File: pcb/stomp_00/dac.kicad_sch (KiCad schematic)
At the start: 6 parts, among them J4 Headphones, U9 SGTL5000XNAA3

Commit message: taking shape...
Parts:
- R1, R2, R3: footprint (none) -> Resistor_SMD:R_0603_1608Metric
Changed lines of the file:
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@@
       (effects (font (size 1.27 1.27)))
     )
-    (property "Footprint" "" (at 125.476 94.996 90)
+    (property "Footprint" "Resistor_SMD:R_0603_1608Metric" (at 125.476 94.996 90)
       (effects (font (size 1.27 1.27)) hide)
     )
@@
       (effects (font (size 1.27 1.27)) (justify right))
     )
-    (property "Footprint" "" (at 99.314 106.426 90)
+    (property "Footprint" "Resistor_SMD:R_0603_1608Metric" (at 99.314 106.426 90)
       (effects (font (size 1.27 1.27)) hide)
     )
@@
       (effects (font (size 1.27 1.27)) (justify right))
     )
-    (property "Footprint" "" (at 90.424 106.426 90)
+    (property "Footprint" "Resistor_SMD:R_0603_1608Metric" (at 90.424 106.426 90)
       (effects (font (size 1.27 1.27)) hide)
     )

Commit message: seeing whether everything will fit...
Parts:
- J4: footprint (none) -> Connector_PinHeader_2.54mm:PinHeader_1x03_P2.54mm_Vertical
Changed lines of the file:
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@@
       (effects (font (size 1.27 1.27)) (justify right))
     )
-    (property "Footprint" "" (at 173.99 86.36 0)
+    (property "Footprint" "Connector_PinHeader_2.54mm:PinHeader_1x03_P2.54mm_Vertical" (at 173.99 86.36 0)
       (effects (font (size 1.27 1.27)) hide)
     )

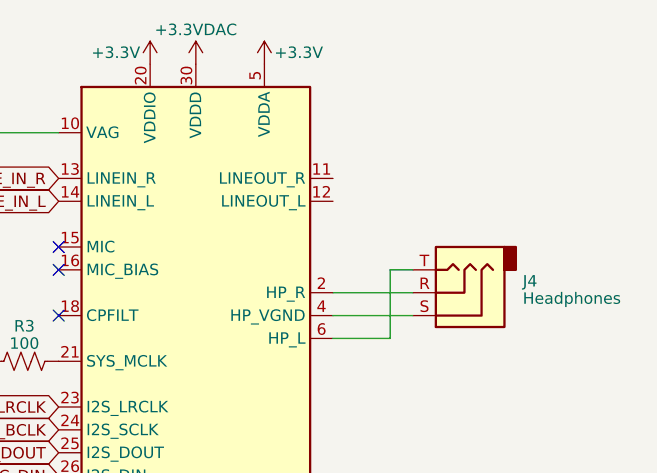
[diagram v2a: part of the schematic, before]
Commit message: input stage schematic
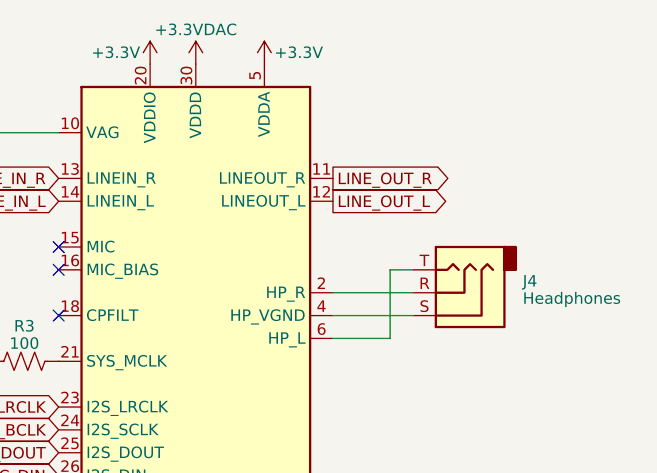
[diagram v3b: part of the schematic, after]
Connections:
- net LINE_OUT_R: now reaches U9.11 (LINEOUT_R)
- net LINE_OUT_L: now reaches U9.12 (LINEOUT_L)
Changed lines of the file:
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@@
     (stroke (width 0) (type default))
+  )
+  (global_label "LINE_OUT_L" (shape output) (at 160.02 76.2 0) (fields_autoplaced)
+    (effects (font (size 1.27 1.27)) (justify left))
+    (property "Intersheetrefs" "${INTERSHEET_REFS}" (at 173.6301 76.2 0)
+      (effects (font (size 1.27 1.27)) (justify left) hide)
+    )
   )
   (global_label "DAC_SCL" (shape input) (at 88.9 114.3 180) (fields_autoplaced)
@@
     )
   )
+  (global_label "LINE_OUT_R" (shape output) (at 160.02 73.66 0) (fields_autoplaced)
+    (effects (font (size 1.27 1.27)) (justify left))
+    (property "Intersheetrefs" "${INTERSHEET_REFS}" (at 173.872 73.66 0)
+      (effects (font (size 1.27 1.27)) (justify left) hide)
+    )
+  )

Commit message: more input stage faffing
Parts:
- added C19, C20, C21, C22: 2.2uF, symbol Device:C_Polarized_US
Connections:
- net LINE_IN_L: now also C20.2; no longer U9.14 (LINEIN_L)
- net LINE_IN_R: now also C19.2; no longer U9.13 (LINEIN_R)
- net LINE_OUT_L: now also C22.2; no longer U9.12 (LINEOUT_L)
- net LINE_OUT_R: now also C21.2; no longer U9.11 (LINEOUT_R)
- new net: C21.1, U9.11 (LINEOUT_R)
- new net: C22.1, U9.12 (LINEOUT_L)
- new net: C19.1, U9.13 (LINEIN_R)
- new net: C20.1, U9.14 (LINEIN_L)
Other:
- moved on the sheet: C6
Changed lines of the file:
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@@
+    (stroke (width 0) (type default))
+  )
+  (wire (pts (xy 160.02 73.66) (xy 198.12 73.66))
     (stroke (width 0) (type default))
   )
@@
     (stroke (width 0) (type default))
   )
+  (wire (pts (xy 110.49 81.915) (xy 115.57 81.915))
+    (stroke (width 0) (type default))
+  )
   (wire (pts (xy 100.33 110.49) (xy 100.33 114.3))
     (stroke (width 0) (type default))
@@
     (stroke (width 0) (type default))
   )
+  (wire (pts (xy 110.49 73.66) (xy 129.54 73.66))
+    (stroke (width 0) (type default))
+  )
   (wire (pts (xy 160.02 91.44) (xy 166.37 91.44))
     (stroke (width 0) (type default))
@@
     (stroke (width 0) (type default))
   )
-  (wire (pts (xy 101.6 68.58) (xy 129.54 68.58))
+  (wire (pts (xy 115.57 76.2) (xy 129.54 76.2))
+    (stroke (width 0) (type default))
+  )
+  (wire (pts (xy 77.47 68.58) (xy 129.54 68.58))
     (stroke (width 0) (type default))
   )
@@
     (stroke (width 0) (type default))
   )
+  (wire (pts (xy 196.215 76.2) (xy 196.215 81.915))
+    (stroke (width 0) (type default))
+  )
+  (wire (pts (xy 160.02 76.2) (xy 196.215 76.2))
+    (stroke (width 0) (type default))
+  )
+  (wire (pts (xy 115.57 76.2) (xy 115.57 81.915))
+    (stroke (width 0) (type default))
+  )
   (wire (pts (xy 166.37 83.82) (xy 168.91 83.82))
     (stroke (width 0) (type default))
@@
     (stroke (width 0) (type default))
   )
+  (wire (pts (xy 196.215 81.915) (xy 198.12 81.915))
+    (stroke (width 0) (type default))
+  )
   (wire (pts (xy 88.9 114.3) (xy 100.33 114.3))
     (stroke (width 0) (type default))
@@
     (stroke (width 0) (type default))
   )
-  (global_label "LINE_OUT_L" (shape output) (at 160.02 76.2 0) (fields_autoplaced)
+  (text_box "Check that this matches the Teensy Audio schematic, doesn't currently!"
+    (at 110.49 35.56 0) (size 37.465 15.24)
+    (stroke (width 0) (type default))
+    (fill (type none))
+    (effects (font (size 1.27 1.27)) (justify left top))
+  )
+  (global_label "LINE_OUT_L" (shape output) (at 205.74 81.915 0) (fields_autoplaced)
     (effects (font (size 1.27 1.27)) (justify left))
-    (property "Intersheetrefs" "${INTERSHEET_REFS}" (at 173.6301 76.2 0)
+    (property "Intersheetrefs" "${INTERSHEET_REFS}" (at 219.3501 81.915 0)
       (effects (font (size 1.27 1.27)) (justify left) hide)
     )
@@
     )
   )
-  (global_label "LINE_OUT_R" (shape output) (at 160.02 73.66 0) (fields_autoplaced)
+  (global_label "LINE_OUT_R" (shape output) (at 205.74 73.66 0) (fields_autoplaced)
     (effects (font (size 1.27 1.27)) (justify left))
-    (property "Intersheetrefs" "${INTERSHEET_REFS}" (at 173.872 73.66 0)
+    (property "Intersheetrefs" "${INTERSHEET_REFS}" (at 219.592 73.66 0)
       (effects (font (size 1.27 1.27)) (justify left) hide)
     )
   )
-  (global_label "LINE_IN_R" (shape input) (at 129.54 73.66 180) (fields_autoplaced)
-    (effects (font (size 1.27 1.27)) (justify right))
-    (property "Intersheetrefs" "${INTERSHEET_REFS}" (at 117.3813 73.66 0)
+  (global_label "LINE_IN_R" (shape input) (at 102.87 73.66 180) (fields_autoplaced)
+    (effects (font (size 1.27 1.27)) (justify right))
+    (property "Intersheetrefs" "${INTERSHEET_REFS}" (at 90.7113 73.66 0)
       (effects (font (size 1.27 1.27)) (justify right) hide)
     )
@@
     )
   )
-  (global_label "LINE_IN_L" (shape input) (at 129.54 76.2 180) (fields_autoplaced)
-    (effects (font (size 1.27 1.27)) (justify right))
-    (property "Intersheetrefs" "${INTERSHEET_REFS}" (at 117.6232 76.2 0)
+  (global_label "LINE_IN_L" (shape input) (at 102.87 81.915 180) (fields_autoplaced)
+    (effects (font (size 1.27 1.27)) (justify right))
+    (property "Intersheetrefs" "${INTERSHEET_REFS}" (at 90.9532 81.915 0)
       (effects (font (size 1.27 1.27)) (justify right) hide)
     )
@@
     )
   )
-  (symbol (lib_id "Device:C_Polarized_US") (at 101.6 72.39 0) (unit 1)
-    (in_bom yes) (on_board yes) (dnp no) (fields_autoplaced)
-    (property "Reference" "C6" (at 104.521 71.1113 0)
+  (symbol (lib_id "Device:C_Polarized_US") (at 77.47 72.39 0) (unit 1)
+    (in_bom yes) (on_board yes) (dnp no) (fields_autoplaced)
+    (property "Reference" "C6" (at 80.391 71.1113 0)
       (effects (font (size 1.27 1.27)) (justify left))
     )
-    (property "Value" "150nF" (at 104.521 73.0323 0)
+    (property "Value" "150nF" (at 80.391 73.0323 0)
       (effects (font (size 1.27 1.27)) (justify left))
     )
-    (property "Footprint" "" (at 101.6 72.39 0)
-      (effects (font (size 1.27 1.27)) hide)
-    )
-    (property "Datasheet" "~" (at 101.6 72.39 0)
+    (property "Footprint" "" (at 77.47 72.39 0)
+      (effects (font (size 1.27 1.27)) hide)
+    )
+    (property "Datasheet" "~" (at 77.47 72.39 0)
       (effects (font (size 1.27 1.27)) hide)
     )
@@
         (path "/8f4a2eb0-078b-46cb-b534-a4acd11d130e/7598c0f0-0137-4b50-80b5-b929d25c284a"
           (reference "C6") (unit 1)
+        )
+      )
+    )
+  )
+  (symbol (lib_id "Device:C_Polarized_US") (at 106.68 81.915 270) (unit 1)
+    (in_bom yes) (on_board yes) (dnp no) (fields_autoplaced)
+    (property "Reference" "C20" (at 107.315 76.7461 90)
+      (effects (font (size 1.27 1.27)))
+    )
+    (property "Value" "2.2uF" (at 107.315 78.6671 90)
+      (effects (font (size 1.27 1.27)))
+    )
+    (property "Footprint" "" (at 106.68 81.915 0)
+      (effects (font (size 1.27 1.27)) hide)
+    )
+    (property "Datasheet" "~" (at 106.68 81.915 0)
+      (effects (font (size 1.27 1.27)) hide)
+    )
+    (pin "1")
+    (pin "2")
+    (instances
+      (project "stomp_00"
+        (path "/8f4a2eb0-078b-46cb-b534-a4acd11d130e/7598c0f0-0137-4b50-80b5-b929d25c284a"
+          (reference "C20") (unit 1)
+        )
+      )
+    )
+  )
+  (symbol (lib_id "Device:C_Polarized_US") (at 201.93 73.66 90) (mirror x) (unit 1)
+    (in_bom yes) (on_board yes) (dnp no) (fields_autoplaced)
+    (property "Reference" "C21" (at 201.295 68.4911 90)
+      (effects (font (size 1.27 1.27)))
+    )
+    (property "Value" "2.2uF" (at 201.295 70.4121 90)
+      (effects (font (size 1.27 1.27)))
+    )
+    (property "Footprint" "" (at 201.93 73.66 0)
+      (effects (font (size 1.27 1.27)) hide)
+    )
+    (property "Datasheet" "~" (at 201.93 73.66 0)
+      (effects (font (size 1.27 1.27)) hide)
+    )
+    (pin "1")
+    (pin "2")
+    (instances
+      (project "stomp_00"
+        (path "/8f4a2eb0-078b-46cb-b534-a4acd11d130e/7598c0f0-0137-4b50-80b5-b929d25c284a"
+          (reference "C21") (unit 1)
         )
       )
@@
     )
   )
-  (symbol (lib_id "power:GND") (at 101.6 76.2 0) (unit 1)
-    (in_bom yes) (on_board yes) (dnp no) (fields_autoplaced)
-    (property "Reference" "#PWR011" (at 101.6 82.55 0)
-      (effects (font (size 1.27 1.27)) hide)
-    )
-    (property "Value" "GND" (at 101.6 80.3355 0)
-      (effects (font (size 1.27 1.27)))
-    )
-    (property "Footprint" "" (at 101.6 76.2 0)
-      (effects (font (size 1.27 1.27)) hide)
-    )
-    (property "Datasheet" "" (at 101.6 76.2 0)
+  (symbol (lib_id "power:GND") (at 77.47 76.2 0) (unit 1)
+    (in_bom yes) (on_board yes) (dnp no) (fields_autoplaced)
+    (property "Reference" "#PWR011" (at 77.47 82.55 0)
+      (effects (font (size 1.27 1.27)) hide)
+    )
+    (property "Value" "GND" (at 77.47 80.3355 0)
+      (effects (font (size 1.27 1.27)))
+    )
+    (property "Footprint" "" (at 77.47 76.2 0)
+      (effects (font (size 1.27 1.27)) hide)
+    )
+    (property "Datasheet" "" (at 77.47 76.2 0)
       (effects (font (size 1.27 1.27)) hide)
     )
@@
         (path "/8f4a2eb0-078b-46cb-b534-a4acd11d130e/7598c0f0-0137-4b50-80b5-b929d25c284a"
           (reference "R2") (unit 1)
+        )
+      )
+    )
+  )
+  (symbol (lib_id "Device:C_Polarized_US") (at 201.93 81.915 90) (mirror x) (unit 1)
+    (in_bom yes) (on_board yes) (dnp no) (fields_autoplaced)
+    (property "Reference" "C22" (at 201.295 76.7461 90)
+      (effects (font (size 1.27 1.27)))
+    )
+    (property "Value" "2.2uF" (at 201.295 78.6671 90)
+      (effects (font (size 1.27 1.27)))
+    )
+    (property "Footprint" "" (at 201.93 81.915 0)
+      (effects (font (size 1.27 1.27)) hide)
+    )
+    (property "Datasheet" "~" (at 201.93 81.915 0)
+      (effects (font (size 1.27 1.27)) hide)
+    )
+    (pin "1")
+    (pin "2")
+    (instances
+      (project "stomp_00"
+        (path "/8f4a2eb0-078b-46cb-b534-a4acd11d130e/7598c0f0-0137-4b50-80b5-b929d25c284a"
+          (reference "C22") (unit 1)
         )
       )
@@
         )
       )
+    )
+  )
+  (symbol (lib_id "Device:C_Polarized_US") (at 106.68 73.66 270) (unit 1)
+    (in_bom yes) (on_board yes) (dnp no) (fields_autoplaced)
+    (property "Reference" "C19" (at 107.315 68.4911 90)
+      (effects (font (size 1.27 1.27)))
+    )
+    (property "Value" "2.2uF" (at 107.315 70.4121 90)
+      (effects (font (size 1.27 1.27)))
+    )
+    (property "Footprint" "" (at 106.68 73.66 0)
+      (effects (font (size 1.27 1.27)) hide)
+    )
+    (property "Datasheet" "~" (at 106.68 73.66 0)
+      (effects (font (size 1.27 1.27)) hide)
+    )
+    (pin "1")
+    (pin "2")
+    (instances
+      (project "stomp_00"
+        (path "/8f4a2eb0-078b-46cb-b534-a4acd11d130e/7598c0f0-0137-4b50-80b5-b929d25c284a"
+          (reference "C19") (unit 1)
+        )
+      )

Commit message: better layout in enclosure
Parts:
- added J2: GuitarOutput1, Connector_Audio:Jack_6.35mm_Neutrik_NMJ4HCD2_Horizontal, symbol Connector_Audio:NMJ4HCD2
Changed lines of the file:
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@@
+    )
+  )
+  (symbol (lib_id "Connector_Audio:NMJ4HCD2") (at 204.47 110.49 0) (mirror x) (unit 1)
+    (in_bom yes) (on_board yes) (dnp no)
+    (property "Reference" "J2" (at 203.835 119.8499 0)
+      (effects (font (size 1.27 1.27)))
+    )
+    (property "Value" "GuitarOutput1" (at 203.835 117.9289 0)
+      (effects (font (size 1.27 1.27)))
+    )
+    (property "Footprint" "Connector_Audio:Jack_6.35mm_Neutrik_NMJ4HCD2_Horizontal" (at 204.47 115.57 0)
+      (effects (font (size 1.27 1.27)) hide)
+    )
+    (property "Datasheet" "https://www.neutrik.com/en/product/nmj4hcd2" (at 204.47 115.57 0)
+      (effects (font (size 1.27 1.27)) hide)
+    )
+    (pin "S")
+    (pin "SN")
+    (pin "T")
+    (pin "TN")
+    (instances
+      (project "stomp_00"
+        (path "/8f4a2eb0-078b-46cb-b534-a4acd11d130e/9942492d-ba8b-45b2-b427-7fe14bedb7e0"
+          (reference "J2") (unit 1)
+        )
+        (path "/8f4a2eb0-078b-46cb-b534-a4acd11d130e/7598c0f0-0137-4b50-80b5-b929d25c284a"
+          (reference "J3") (unit 1)
+        )
+      )
     )
   )

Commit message: footswitch routing
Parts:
- removed J2: GuitarOutput1, Connector_Audio:Jack_6.35mm_Neutrik_NMJ4HCD2_Horizontal, symbol Connector_Audio:NMJ4HCD2
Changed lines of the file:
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@@
-    )
-  )
-  (symbol (lib_id "Connector_Audio:NMJ4HCD2") (at 204.47 110.49 0) (mirror x) (unit 1)
-    (in_bom yes) (on_board yes) (dnp no)
-    (property "Reference" "J2" (at 203.835 119.8499 0)
-      (effects (font (size 1.27 1.27)))
-    )
-    (property "Value" "GuitarOutput1" (at 203.835 117.9289 0)
-      (effects (font (size 1.27 1.27)))
-    )
-    (property "Footprint" "Connector_Audio:Jack_6.35mm_Neutrik_NMJ4HCD2_Horizontal" (at 204.47 115.57 0)
-      (effects (font (size 1.27 1.27)) hide)
-    )
-    (property "Datasheet" "https://www.neutrik.com/en/product/nmj4hcd2" (at 204.47 115.57 0)
-      (effects (font (size 1.27 1.27)) hide)
-    )
-    (pin "S")
-    (pin "SN")
-    (pin "T")
-    (pin "TN")
-    (instances
-      (project "stomp_00"
-        (path "/8f4a2eb0-078b-46cb-b534-a4acd11d130e/9942492d-ba8b-45b2-b427-7fe14bedb7e0"
-          (reference "J2") (unit 1)
-        )
-        (path "/8f4a2eb0-078b-46cb-b534-a4acd11d130e/7598c0f0-0137-4b50-80b5-b929d25c284a"
-          (reference "J3") (unit 1)
-        )
-      )
     )
   )

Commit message: pcb...
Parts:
- added C5, C8: 1uF, Capacitor_SMD:C_0603_1608Metric, symbol Device:C
- added FB1: 600, Inductor_SMD:L_0603_1608Metric, symbol Device:FerriteBead
- added U11: AP7313-18SAG, Package_TO_SOT_SMD:SOT-23, symbol Regulator_Linear:SPX2920M3-3.3_SOT223
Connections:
- net +3.3V: now also C5.1, FB1.1, U11.1 (VI); no longer U9.5 (VDDA)
- net GND: now also C5.2, C8.2, U11.3 (GND)
- net +3.3VDAC renamed +1V8
- net +1V8: now also C8.1, U11.2 (VO)
- new net: FB1.2, U9.5 (VDDA)
